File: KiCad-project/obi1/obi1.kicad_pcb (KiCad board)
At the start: 4 copper layers, 64 x 70 mm, 134 parts, among them IC1 RAM, IC2 DAC, IC3 IMU, IC4 FLASH, J1 USB, J2 JTAG-H, J3 Conn_01x04, J4 Conn_01x04, J5 Conn_01x10, J6 Conn_01x10, J7 Conn_02x11_Counter_Clockwise, J8 Conn_02x17_Counter_Clockwise, SW1 SW_Push, SW2 SW_Push, SW3 SW_DIP_x08, U1 RG3V3, U2 REG1V2, U3 XC6SLX16-FTG256, U4 OSC, U5 ADC, U6 RV1, U7 RV2

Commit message: Routear
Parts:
- removed the IC3 at (177.2, 94.7)
- added C53: @0.47uF;6.3V;X5R;0402;10%, Capacitor_SMD:C_0402_1005Metric_Pad0.74x0.62mm_HandSolder, F.Cu at (153.5, 117.0)
- added C54: @0.47uF;6.3V;X5R;0402;10%, Capacitor_SMD:C_0402_1005Metric_Pad0.74x0.62mm_HandSolder, F.Cu at (156.0, 117.0)
- added C55: @4.7uF;6.3V;X5R;0805;10%, Capacitor_SMD:C_0805_2012Metric_Pad1.18x1.45mm_HandSolder, F.Cu at (194.7, 111.7)
- added R48: @100;1/4W;0805;1%, Resistor_SMD:R_0805_2012Metric_Pad1.20x1.40mm_HandSolder, F.Cu at (163.6, 113.9)
- added R49: @100;1/4W;0805;1%, Resistor_SMD:R_0805_2012Metric_Pad1.20x1.40mm_HandSolder, F.Cu at (199.5, 111.6)
- added U6: BMF055, Package_LGA:LGA-28_5.2x3.8mm_P0.5mm, F.Cu at (199.5, 94.2)
- C1: value 4.7uf -> @4.7uF;6.3V;X5R;0805;10%; footprint Capacitor_SMD:C_0805_2012Metric -> Capacitor_SMD:C_0805_2012Metric_Pad1.18x1.45mm_HandSolder
- C10, C14, C16, C19, C24, C28, C29, C30, C31, C32, C33, C36, C46, C7: value 4.7uF -> @4.7uF;6.3V;X5R;0805;10%; footprint Capacitor_SMD:C_0805_2012Metric -> Capacitor_SMD:C_0805_2012Metric_Pad1.18x1.45mm_HandSolder
- C11, C12, C17, C20, C21, C22, C25, C26, C27, C34, C35, C50, C51, C8: value 0.47uF -> @0.47uF;6.3V;X5R;0402;10%; footprint Capacitor_SMD:C_0805_2012Metric -> Capacitor_SMD:C_0402_1005Metric_Pad0.74x0.62mm_HandSolder
- C13: value 0.01uF -> @0.01uF;6.3V;X7R;0805;10%; footprint Capacitor_SMD:C_0805_2012Metric -> Capacitor_SMD:C_0805_2012Metric_Pad1.18x1.45mm_HandSolder
- C15, C18, C23, C6, C9: value 100uF -> @100uF;6.3V;X5R;1210;20%; footprint Capacitor_SMD:C_0805_2012Metric -> Capacitor_SMD:C_1210_3225Metric_Pad1.33x2.70mm_HandSolder
- C2, C3, C4, C5: value 1uf -> @1uF;6.3V;X5R;0805;10%; footprint Capacitor_SMD:C_0805_2012Metric -> Capacitor_SMD:C_0805_2012Metric_Pad1.18x1.45mm_HandSolder
- C37: value 10uF -> @10uF;6.3V;X5R;0805;20%; footprint Capacitor_SMD:C_0805_2012Metric -> Capacitor_SMD:C_0805_2012Metric_Pad1.18x1.45mm_HandSolder
- C38: value 1uF -> @1uF;6.3V;X5R;0805;10%; footprint Capacitor_SMD:C_0805_2012Metric -> Capacitor_SMD:C_0805_2012Metric_Pad1.18x1.45mm_HandSolder
- C39, C40: value 0.1uF -> @0.1uF;6.3V;X5R;0805;10%; footprint Capacitor_SMD:C_0805_2012Metric -> Capacitor_SMD:C_0805_2012Metric_Pad1.18x1.45mm_HandSolder
- C41: value 100nF -> @0.1uF;6.3V;X5R;0805;10%; footprint Capacitor_SMD:C_0805_2012Metric -> Capacitor_SMD:C_0805_2012Metric_Pad1.18x1.45mm_HandSolder
- C42: value 100nF -> @1uF;6.3V;X5R;0805;10%; footprint Capacitor_SMD:C_0805_2012Metric -> Capacitor_SMD:C_0805_2012Metric_Pad1.18x1.45mm_HandSolder
- C43: value 4.7uF -> @1uF;6.3V;X5R;0805;10%; footprint Capacitor_SMD:C_0805_2012Metric -> Capacitor_SMD:C_0805_2012Metric_Pad1.18x1.45mm_HandSolder
- C44: value 4.7uF -> @0.12uF;10V;X7R;0603;10%; footprint Capacitor_SMD:C_0805_2012Metric -> Capacitor_SMD:C_0603_1608Metric_Pad1.08x0.95mm_HandSolder
- C45: value 4.7uF -> @6800pF;10V;X7R;0603;10%; footprint Capacitor_SMD:C_0805_2012Metric -> Capacitor_SMD:C_0603_1608Metric_Pad1.08x0.95mm_HandSolder
- C47, C48, C49: value 0.47uF -> @4.7uF;6.3V;X5R;0805;10%; footprint Capacitor_SMD:C_0805_2012Metric -> Capacitor_SMD:C_0805_2012Metric_Pad1.18x1.45mm_HandSolder
- C52: value 4.7uF -> @0.47uF;6.3V;X5R;0402;10%; footprint Capacitor_SMD:C_0805_2012Metric -> Capacitor_SMD:C_0402_1005Metric_Pad0.74x0.62mm_HandSolder
- D1: value DONE -> @DONE;LED;GRE;0603; footprint LED_SMD:LED_0805_2012Metric -> LED_SMD:LED_0603_1608Metric_Pad1.05x0.95mm_HandSolder
- D2, D3, D4, D5, D6, D7, D8, D9: value G -> @LED;BLU;0603; footprint LED_SMD:LED_0805_2012Metric -> LED_SMD:LED_0603_1608Metric_Pad1.05x0.95mm_HandSolder
- R1: value 1M -> @1M;1/2W;0805;1%; footprint Resistor_SMD:R_0805_2012Metric -> Resistor_SMD:R_0805_2012Metric_Pad1.20x1.40mm_HandSolder
- R10: value 4K7 -> @4.7K;1/4W;0805;1%; footprint Resistor_SMD:R_0805_2012Metric -> Resistor_SMD:R_0805_2012Metric_Pad1.20x1.40mm_HandSolder
- R11: value 330 -> @330;1/4W;0805;1%; footprint Resistor_SMD:R_0805_2012Metric -> Resistor_SMD:R_0805_2012Metric_Pad1.20x1.40mm_HandSolder
- R12, R2, R3, R37, R38, R4, R40, R41, R5, R6, R7, R8, R9: value 100 -> @100;1/4W;0805;1%; footprint Resistor_SMD:R_0805_2012Metric -> Resistor_SMD:R_0805_2012Metric_Pad1.20x1.40mm_HandSolder
- R13, R14, R15, R16, R17, R18: value 4.7K -> @51;1/4W;0805;5%; footprint Resistor_SMD:R_0805_2012Metric -> Resistor_SMD:R_0805_2012Metric_Pad1.20x1.40mm_HandSolder
- R19: value 4.7K -> @20;1/4W;0805;1%; footprint Resistor_SMD:R_0805_2012Metric -> Resistor_SMD:R_0805_2012Metric_Pad1.20x1.40mm_HandSolder; moved to F.Cu
- R20: value 4.7K -> @10K;1/4W;0805;1%; footprint Resistor_SMD:R_0805_2012Metric -> Resistor_SMD:R_0805_2012Metric_Pad1.20x1.40mm_HandSolder
- R21, R22, R23, R24, R25, R26: value 50 -> @4.7K;1/4W;0805;1%; footprint Resistor_SMD:R_0805_2012Metric -> Resistor_SMD:R_0805_2012Metric_Pad1.20x1.40mm_HandSolder
- R27, R28: value 20 -> @4.7K;1/4W;0805;1%; footprint Resistor_SMD:R_0805_2012Metric -> Resistor_SMD:R_0805_2012Metric_Pad1.20x1.40mm_HandSolder
- R29, R30, R31, R32, R33, R34, R35: value 100 -> @20;1/4W;0805;1%; footprint Resistor_SMD:R_0805_2012Metric -> Resistor_SMD:R_0805_2012Metric_Pad1.20x1.40mm_HandSolder; moved to B.Cu
- R36: value 100 -> @20;1/4W;0805;1%; footprint Resistor_SMD:R_0805_2012Metric -> Resistor_SMD:R_0805_2012Metric_Pad1.20x1.40mm_HandSolder
- R39: value 2K4 -> @100;1/4W;0805;1%; footprint Resistor_SMD:R_0805_2012Metric -> Resistor_SMD:R_0805_2012Metric_Pad1.20x1.40mm_HandSolder
- R42, R43, R44, R45, R46: value 20 -> @100;1/4W;0805;1%; footprint Resistor_SMD:R_0805_2012Metric -> Resistor_SMD:R_0805_2012Metric_Pad1.20x1.40mm_HandSolder; moved to F.Cu
- R47: value 20 -> @2.4K;1/4W;0805;1%; footprint Resistor_SMD:R_0805_2012Metric -> Resistor_SMD:R_0805_2012Metric_Pad1.20x1.40mm_HandSolder; moved to F.Cu
- moved R19 75.1 mm to (203.1, 98.5), turned to 0 degrees
- moved R24 68.1 mm to (128.7, 112.4)
- moved R18 66.5 mm to (180.7, 68.5)
- moved R14 65.0 mm to (173.9, 73.4)
- moved R23 65.0 mm to (128.7, 115.1), turned to 180 degrees
- moved R17 63.1 mm to (174.0, 68.5), turned to 0 degrees
- moved R26 56.7 mm to (128.7, 107.6)
- moved R25 54.1 mm to (128.7, 109.9)
- moved R16 52.9 mm to (180.6, 125.3), turned to 0 degrees
- moved R13 52.5 mm to (181.1, 122.9)
- moved R22 52.5 mm to (128.7, 117.7), turned to 180 degrees
- moved R15 51.5 mm to (179.1, 128.4), turned to 0 degrees
- moved R21 51.1 mm to (128.7, 120.1), turned to 180 degrees
- moved C52 47.1 mm to (175.5, 74.2), turned to 180 degrees
- moved C44 43.7 mm to (210.0, 92.7), turned to 0 degrees
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- renumbered IC4 to IC3, J8 to J7, J7 to J8, U6 to U7, U7 to U8
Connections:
- C43 pad 1: +3V3 -> Net-(C43-Pad1)
- C45 pad 1: +5V -> +3V3
- C46 pad 1: +5V -> +3V3
- C48 pad 1: +3V3 -> +5V
- C50 pad 1: +5V -> +3V3
- C51 pad 1: GND -> +3V3
- C51 pad 2: +3V3 -> GND
- C52 pad 1: GND -> +5V
- C52 pad 2: +3V3 -> GND
- F1 pad 2: Net-(F1-Pad2) -> (no net)
- IC3 pad 2: Net-(IC4-Pad2) -> Net-(IC3-Pad2)
- IC3 pad 3: Net-(IC4-Pad3) -> Net-(IC3-Pad3)
- IC3 pad 5: Net-(IC4-Pad5) -> Net-(IC3-Pad5)
- IC3 pad 7: Net-(IC4-Pad7) -> Net-(IC3-Pad7)
- J1 pad 4: Net-(F1-Pad2) -> +5V
- J7 pad 1: IO_C02 -> (no net)
- J7 pad 2: IO_C04 -> (no net)
- J7 pad 3: IO_C06 -> (no net)
- J7 pad 4: IO_C03 -> (no net)
- J8 pad 3: IO_C00 -> (no net)
- J8 pad 5: IO_C01 -> (no net)
- R13 pad 1: DS_1 -> Net-(IC2-Pad4)
- R13 pad 2: GND -> DAC_SCK
- R14 pad 1: DS_2 -> Net-(R14-Pad1)
- R14 pad 2: GND -> ADC_SCLK
- R15 pad 1: DS_3 -> Net-(J3-Pad1)
- R15 pad 2: GND -> DAC_VOUTA
- R16 pad 1: DS_4 -> Net-(J3-Pad4)
- R16 pad 2: GND -> DAC_VOUTB
- R17 pad 1: DS_5 -> Net-(J4-Pad1)
- R17 pad 2: GND -> ADC_IN1
- R18 pad 1: DS_6 -> Net-(J4-Pad4)
- R18 pad 2: GND -> ADC_IN2
- R19 pad 1: DS_7 -> +3V3
- R19 pad 2: GND -> nReset
- R20 pad 1: DS_8 -> Net-(R20-Pad1)
- R20 pad 2: GND -> +3V3
- R21 pad 1: Net-(J3-Pad1) -> DS_1
- R21 pad 2: DAC_VOUTA -> GND
- R22 pad 1: Net-(J3-Pad4) -> DS_2
- R22 pad 2: DAC_VOUTB -> GND
- R23 pad 1: Net-(J4-Pad1) -> DS_3
- R23 pad 2: ADC_IN1 -> GND
- R24 pad 1: Net-(J4-Pad4) -> DS_4
- R24 pad 2: ADC_IN2 -> GND
- R25 pad 1: Net-(IC2-Pad4) -> DS_5
- R25 pad 2: DAC_SCK -> GND
- R26 pad 1: Net-(R26-Pad1) -> DS_6
- R26 pad 2: ADC_SCLK -> GND
- R27 pad 1: IO_B03 -> DS_7
- R27 pad 2: DS_1 -> GND
- R28 pad 1: IO_B05 -> DS_8
- R28 pad 2: DS_2 -> GND
- R29 pad 1: Net-(D2-Pad2) -> IO_B03
- R29 pad 2: LED_1 -> DS_1
- R30 pad 1: Net-(D3-Pad2) -> IO_B05
- R30 pad 2: LED_2 -> DS_2
- R31 pad 1: Net-(D4-Pad2) -> IO_D04
- R31 pad 2: LED_3 -> DS_3
- R32 pad 1: Net-(D5-Pad2) -> IO_A07
- R32 pad 2: LED_4 -> DS_4
- R33 pad 1: Net-(D6-Pad2) -> IO_A04
- R33 pad 2: LED_5 -> DS_5
- R34 pad 1: Net-(D7-Pad2) -> IO_B00
- R34 pad 2: LED_6 -> DS_6
- R35 pad 1: Net-(D8-Pad2) -> IO_D01
- R35 pad 2: LED_7 -> DS_7
- R36 pad 1: Net-(D9-Pad2) -> IO_D05
- R36 pad 2: LED_8 -> DS_8
- R37 pad 1: Net-(IC4-Pad3) -> Net-(D2-Pad2)
- R37 pad 2: XC_N12 -> LED_1
- R38 pad 1: Net-(IC4-Pad2) -> Net-(D3-Pad2)
- R38 pad 2: XC_P10 -> LED_2
- R39 pad 1: +3V3 -> Net-(D4-Pad2)
- R39 pad 2: XC_T3 -> LED_3
- R40 pad 1: XC_P12 -> Net-(D5-Pad2)
- R40 pad 2: Net-(IC4-Pad7) -> LED_4
- R41 pad 1: XC_T10 -> Net-(D6-Pad2)
- R41 pad 2: Net-(IC4-Pad5) -> LED_5
- R42 pad 1: IO_D04 -> Net-(D7-Pad2)
- R42 pad 2: DS_3 -> LED_6
- R43 pad 1: IO_A07 -> Net-(D8-Pad2)
- R43 pad 2: DS_4 -> LED_7
- R44 pad 1: IO_A04 -> Net-(D9-Pad2)
- R44 pad 2: DS_5 -> LED_8
- R45 pad 1: IO_B00 -> Net-(IC3-Pad3)
- R45 pad 2: DS_6 -> XC_N12
- R46 pad 1: IO_D01 -> Net-(IC3-Pad2)
- R46 pad 2: DS_7 -> XC_P10
- R47 pad 1: IO_D05 -> +3V3
- R47 pad 2: DS_8 -> XC_T3
- U3 pad A9: OSC_ED -> (no net)
- U3 pad C15: IMU_CSB2 -> IMU_PA31
- U3 pad C16: IMU_DRDYM -> IMU_PA30
- U3 pad D16: IMU_INT2 -> IMU_PA18
- U3 pad E13: IO_C06 -> nReset
- U3 pad E15: IMU_INT1 -> IMU_PA28
- U3 pad E16: IMU_CSB3 -> IMU_PA27
- U3 pad F12: (no net) -> IMU_PB00
- U3 pad F13: IO_C03 -> IMU_PA17
- U3 pad F14: IO_C02 -> IMU_PA16
- U3 pad F15: IMU_CSB1 -> IMU_PA24
- U3 pad F16: IMU_MISO -> IMU_PA23
- U3 pad G11: IO_C04 -> IMU_PB01
- U3 pad G12: (no net) -> IMU_PB02
- U3 pad G14: IMU_INT3 -> IMU_PA22
- U3 pad G16: IMU_INT4 -> IMU_PA21
- U3 pad H11: IO_C00 -> IMU_PB03
- U3 pad H13: IO_C01 -> IMU_PB16
- U3 pad H15: IMU_INT5 -> IMU_PA20
- U3 pad H16: IMU_SDX -> IMU_PA19
- U3 pad J12: (no net) -> IMU_PB17
- U3 pad J14: (no net) -> IMU_PB23
- U4 pad 1: OSC_ED -> +3V3
- U5 pad 8: Net-(R26-Pad1) -> Net-(R14-Pad1)
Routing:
- net IO_C00: track 72.3 -> 0.00 mm, vias 1 -> 0
- net IMU_PB03: track 0.00 -> 72.3 mm, vias 0 -> 1
- net IO_C01: track 70.4 -> 0.00 mm, vias 1 -> 0
- net IMU_PB16: track 0.00 -> 70.4 mm, vias 0 -> 1
- net nReset: track 0.00 -> 59.1 mm, vias 0 -> 9
- net IO_C04: track 35.3 -> 0.00 mm, vias 1 -> 0
- net IMU_PB01: track 0.00 -> 35.3 mm, vias 0 -> 1
- net IO_C03: track 33.4 -> 0.00 mm, vias 1 -> 0
- net IMU_PA17: track 0.00 -> 33.4 mm, vias 0 -> 1
- net IO_C02: track 28.8 -> 0.00 mm, vias 1 -> 0
- net IMU_PA16: track 0.00 -> 28.8 mm, vias 0 -> 1
- net IO_C06: track 28.7 -> 0.00 mm, vias 1 -> 0
- net +3V3: track 157.6 -> 130.7 mm, vias 89 -> 79
- net IMU_PA31: track 0.00 -> 17.4 mm
- net IMU_CSB2: track 17.4 -> 0.00 mm
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- added copper zone on VCC, net nReset
- removed copper zone on VCC, net +3V3
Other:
- net class Default: clearance 0.1321 -> 0.1524; trace_width 0.1321 -> 0.1524; via_dia 0.4 -> 0.61; via_drill 0.2 -> 0.3
- net class PWR: clearance 0.127 -> 0.1524; trace_width 0.381 -> 0.4; via_dia 0.4 -> 0.61; via_drill 0.2 -> 0.3
- rule trace_clearance: 0.1321 -> 0.1524
- rule trace_min: 0.13 -> 0.1524
- rule via_min_drill: 0.2 -> 0.3
- rule via_min_size: 0.4 -> 0.61

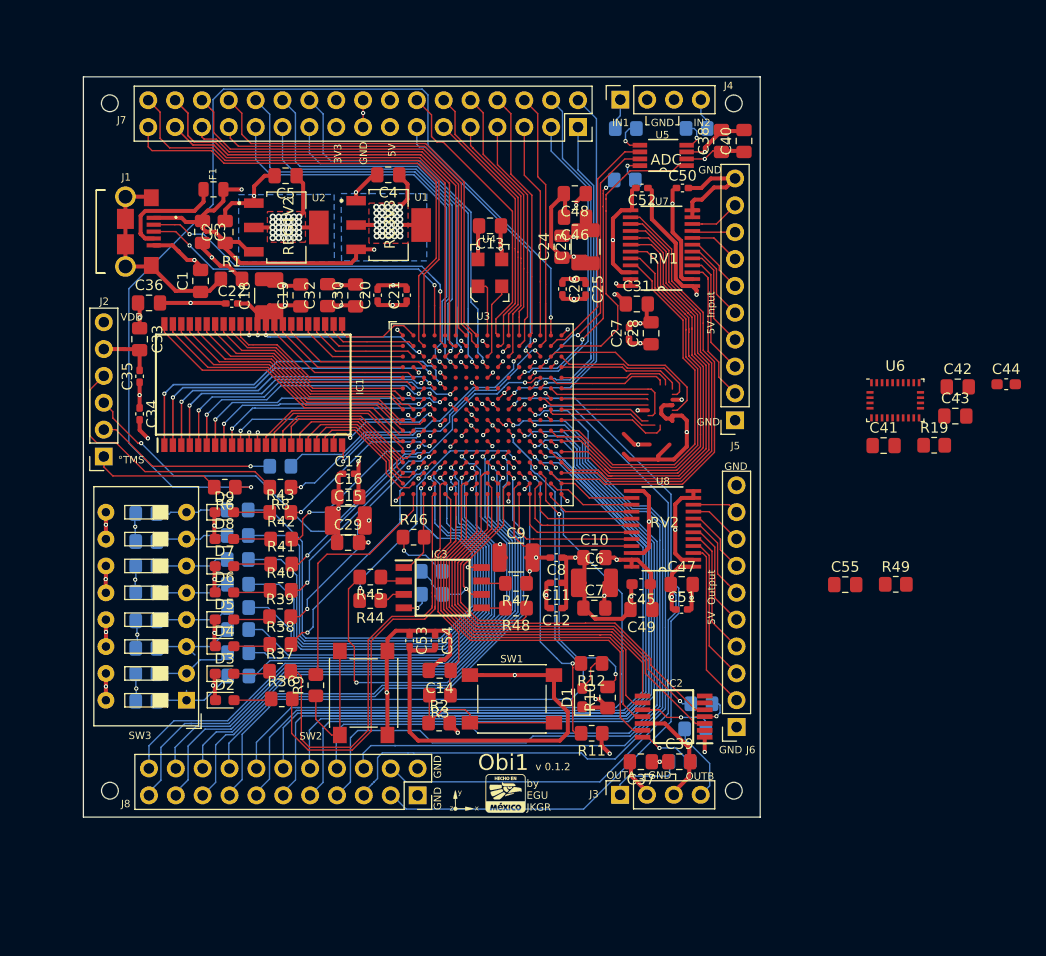
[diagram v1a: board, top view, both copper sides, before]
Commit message: Resize board, change layout, re-route IO pins, new imu added
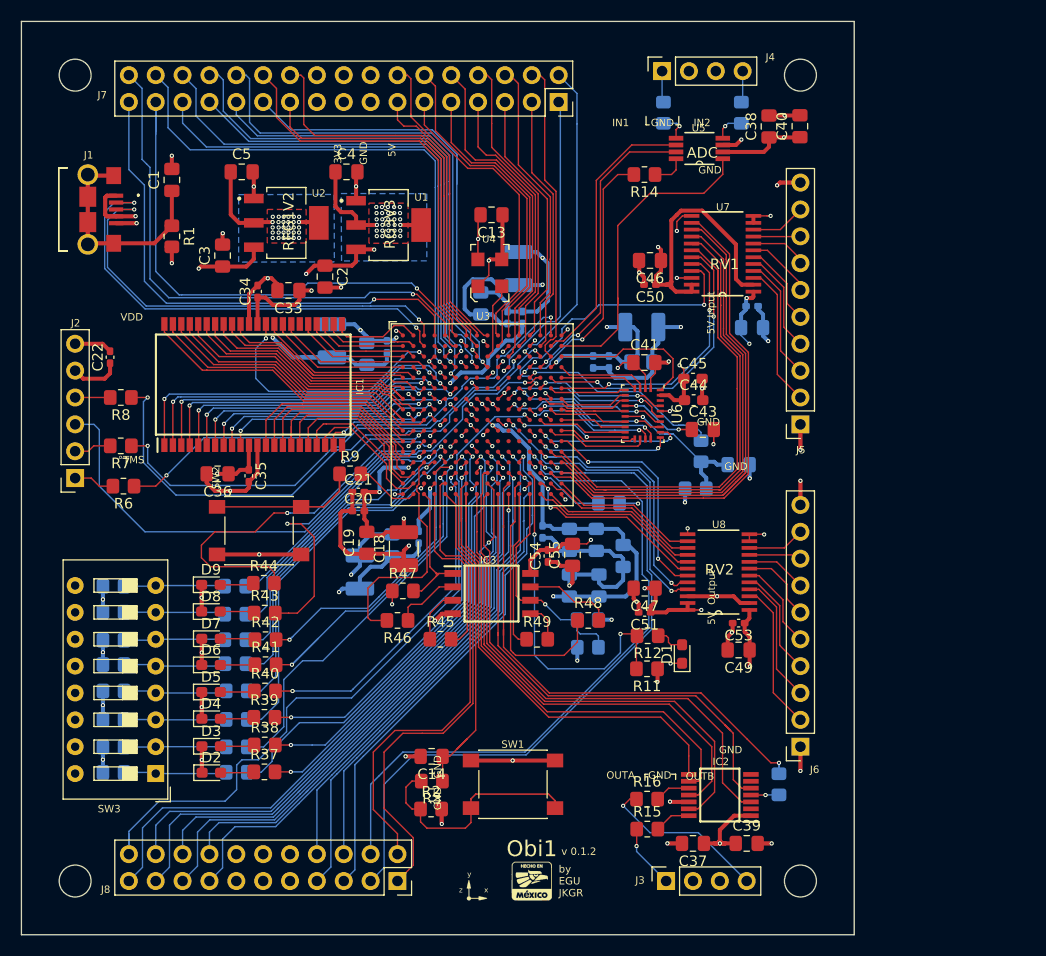
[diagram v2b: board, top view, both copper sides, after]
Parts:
- removed F1: Fuse, Fuse:Fuse_0805_2012Metric
- C10, C11, C12, C15, C16, C17, C23, C24, C25, C26, C27, C28, C29, C30, C31, C32, C42, C48, C52, C6, C7, C8, C9, R10, R36: moved to B.Cu
- R14, R15, R16, R7: moved to F.Cu
- R19: value @20;1/4W;0805;1% -> @10;1/4W;0805;1%; moved to B.Cu
- moved R20 55.7 mm to (180.6, 102.6), turned to 0 degrees
- moved C32 35.7 mm to (168.7, 111.8), turned to 270 degrees
- moved C30 35.3 mm to (173.7, 109.0)
- moved R49 34.3 mm to (165.6, 116.8)
- moved C6 33.8 mm to (146.2, 88.6), turned to 90 degrees
- moved C7 32.3 mm to (149.5, 89.9), turned to 90 degrees
- moved C53 31.2 mm to (184.7, 115.3), turned to 180 degrees
- moved C44 29.6 mm to (180.4, 94.2)
- moved C18 27.1 mm to (153.0, 108.3)
- moved C31 26.9 mm to (171.4, 111.8), turned to 270 degrees
- moved C55 25.9 mm to (168.9, 108.9), turned to 90 degrees
- moved C8 25.6 mm to (151.4, 89.2), turned to 90 degrees
- moved C9 24.8 mm to (175.5, 87.3), turned to 180 degrees
- moved C19 24.2 mm to (149.5, 107.7)
- moved C41 23.9 mm to (175.7, 90.7)
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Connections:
- C42 pad 1: +3V3 -> Net-(C42-Pad1)
- J7 pad 1: (no net) -> IO_C01
- J7 pad 10: IO_I00 -> IO_D03
- J7 pad 11: IO_G03 -> IO_D04
- J7 pad 12: IO_H04 -> IO_D05
- J7 pad 13: IO_I01 -> IO_D06
- J7 pad 14: IO_G04 -> IO_D07
- J7 pad 15: +5V -> +3V3
- J7 pad 16: +5V -> +3V3
- J7 pad 19: +3V3 -> +5V
- J7 pad 2: (no net) -> IO_C02
- J7 pad 20: +3V3 -> +5V
- J7 pad 21: IO_H01 -> IO_E01
- J7 pad 22: IO_H06 -> IO_E02
- J7 pad 23: IO_F00 -> IO_E03
- J7 pad 24: IO_G00 -> IO_E04
- J7 pad 25: IO_E07 -> IO_E05
- J7 pad 26: IO_F07 -> IO_E06
- J7 pad 27: IO_G01 -> IO_E07
- J7 pad 28: IO_G02 -> IO_F01
- J7 pad 3: (no net) -> IO_C03
- J7 pad 30: IO_F06 -> IO_F03
- J7 pad 31: IO_D02 -> IO_F04
- J7 pad 32: IO_F01 -> IO_F05
- J7 pad 33: IO_B04 -> IO_F06
- J7 pad 34: IO_B07 -> IO_F07
- J7 pad 4: (no net) -> IO_C04
- J7 pad 5: IO_I06 -> IO_C05
- J7 pad 6: IO_I05 -> IO_C06
- J7 pad 7: IO_H07 -> IO_C07
- J7 pad 8: IO_I02 -> IO_D01
- J7 pad 9: IO_H03 -> IO_D02
- J8 pad 1: GND -> IO_A00
- J8 pad 10: IO_E04 -> +3V3
- J8 pad 11: IO_E02 -> GND
- J8 pad 12: IO_E06 -> GND
- J8 pad 13: IO_E05 -> +5V
- J8 pad 14: IO_E01 -> +5V
- J8 pad 15: DS_2_XC7 -> IO_B00
- J8 pad 16: IO_A02 -> IO_B01
- J8 pad 17: IO_A01 -> IO_B02
- J8 pad 18: IO_A03 -> IO_B03
- J8 pad 19: IO_A06 -> IO_B04
- J8 pad 2: GND -> IO_A01
- J8 pad 20: IO_B01 -> IO_B05
- J8 pad 22: IO_B02 -> IO_B07
- J8 pad 3: (no net) -> IO_A02
- J8 pad 4: DS_2_XC1 -> IO_A03
- J8 pad 5: (no net) -> IO_A04
- J8 pad 6: DS_2_XC2 -> IO_A05
- J8 pad 7: DS_2_XC4 -> IO_A06
- J8 pad 8: DS_2_XC6 -> IO_A07
- J8 pad 9: DS_2_XC5 -> +3V3
- R19 pad 1: +3V3 -> Net-(C42-Pad1)
- R20 pad 1: Net-(R20-Pad1) -> +3V3
- R20 pad 2: +3V3 -> Net-(C42-Pad1)
- R29 pad 1: IO_B03 -> DS_2_XC1
- R30 pad 1: IO_B05 -> DS_2_XC2
- R31 pad 1: IO_D04 -> DS_2_XC3
- R32 pad 1: IO_A07 -> DS_2_XC4
- R33 pad 1: IO_A04 -> DS_2_XC5
- R34 pad 1: IO_B00 -> DS_2_XC6
- R35 pad 1: IO_D01 -> DS_2_XC7
- R36 pad 1: IO_D05 -> DS_2_XC8
- U3 pad A10: IO_G04 -> IO_D04
- U3 pad A11: IO_H04 -> IO_D02
- U3 pad A12: IO_I00 -> IO_C07
- U3 pad A13: IO_I02 -> IO_C05
- U3 pad A14: IO_I06 -> IO_C06
- U3 pad A3: IO_B07 -> D+
- U3 pad A4: D+ -> IO_F06
- U3 pad A5: IO_D02 -> IO_F07
- U3 pad A6: IO_F02 -> IO_E04
- U3 pad A7: IO_F06 -> IO_E01
- U3 pad A8: IO_G02 -> IO_D06
- U3 pad A9: (no net) -> IO_D07
- U3 pad B10: IO_G03 -> IO_D05
- U3 pad B12: IO_H07 -> IO_D01
- U3 pad B14: IO_I05 -> IO_C03
- U3 pad B3: IO_B04 -> D-
- U3 pad B5: D- -> (no net)
- U3 pad B6: IO_F01 -> IO_F04
- U3 pad B8: IO_G01 -> IO_E02
- U3 pad C11: IO_H03 -> IO_D03
- U3 pad C13: IO_I01 -> IO_C02
- U3 pad C15: IMU_PA31 -> IO_C04
- U3 pad C16: IMU_PA30 -> IMU_PB03
- U3 pad C5: IO_F00 -> IO_F03
- U3 pad C6: IO_G00 -> IO_F01
- U3 pad C8: (no net) -> IO_E06
- U3 pad D11: (no net) -> IO_C01
- U3 pad D16: IMU_PA18 -> IMU_PB02
- U3 pad D5: IO_E07 -> IO_F05
- U3 pad D6: IO_F07 -> IO_F02
- U3 pad D8: IO_H01 -> IO_E05
- U3 pad D9: IO_H06 -> IO_E03
- U3 pad E15: IMU_PA28 -> 3v3_2_XC02
- U3 pad E16: IMU_PA27 -> IMU_PB01
- U3 pad E6: (no net) -> IO_E07
- U3 pad F12: IMU_PB00 -> IMU_PA17
- U3 pad F13: IMU_PA17 -> 3v3_2_XC00
- U3 pad F14: IMU_PA16 -> IMU_SCX
- U3 pad F15: IMU_PA24 -> IMU_PB00
- U3 pad F16: IMU_PA23 -> 3v3_2_XC01
- U3 pad G11: IMU_PB01 -> IMU_PA16
- U3 pad G12: IMU_PB02 -> (no net)
- U3 pad G14: IMU_PA22 -> IMU_PA30
- U3 pad G16: IMU_PA21 -> IMU_PA31
- U3 pad H11: IMU_PB03 -> IMU_PA18
- U3 pad H13: IMU_PB16 -> IMU_PA20
- U3 pad H14: DS_2_XC1 -> IMU_PB17
- U3 pad H15: IMU_PA20 -> IMU_PA27
- U3 pad H16: IMU_PA19 -> IMU_PA28
- U3 pad J11: DS_2_XC2 -> 3v3_2_XC08
- U3 pad J12: IMU_PB17 -> IMU_PA23
- U3 pad J13: DS_2_XC4 -> IO_B07
- U3 pad J14: IMU_PB23 -> IMU_PA24
- U3 pad J16: IMU_SCX -> IMU_PB23
- U3 pad K11: DS_2_XC7 -> (no net)
- U3 pad K12: DS_2_XC6 -> (no net)
- U3 pad K14: DS_2_XC5 -> IMU_PA19
- U3 pad K15: 3v3_2_XC01 -> IMU_PA21
- U3 pad K16: 3v3_2_XC00 -> IMU_PA22
- U3 pad L13: IO_E04 -> (no net)
- U3 pad L14: IO_E02 -> IMU_PB16
- U3 pad L16: 3v3_2_XC02 -> 3v3_2_XC10
- U3 pad M10: IO_A06 -> IO_B01
- U3 pad M11: IO_A01 -> IO_A06
- U3 pad M13: IO_E05 -> IO_A03
- U3 pad M14: IO_E06 -> 3v3_2_XC09
- U3 pad M3: LED_6 -> DS_2_XC8
- U3 pad M4: LED_5 -> DS_2_XC7
- U3 pad M5: (no net) -> DS_2_XC6
- U3 pad M6: (no net) -> LED_6
- U3 pad M7: IO_B06 -> LED_2
- U3 pad M9: IO_B01 -> IO_B03
- U3 pad N11: GND -> (no net)
- U3 pad N12: XC_N12 -> IO_A04
- U3 pad N14: IO_E01 -> IO_A02
- U3 pad N3: LED_4 -> XC_P10
- U3 pad N4: LED_3 -> DS_2_XC5
- U3 pad N5: IO_B00 -> DS_2_XC4
- U3 pad N6: IO_D04 -> DS_2_XC1
- U3 pad N8: IO_B02 -> IO_B06
- U3 pad N9: IO_A03 -> IO_B04
- U3 pad P10: XC_P10 -> IO_B02
- U3 pad P11: IO_A02 -> IO_A07
- U3 pad P12: XC_P12 -> IO_A05
- U3 pad P4: IO_D01 -> DS_2_XC2
- U3 pad P5: IO_A04 -> LED_5
- U3 pad P6: IO_A07 -> LED_4
- U3 pad P7: IO_B05 -> LED_3
- U3 pad P8: IO_B03 -> LED_1
- U3 pad P9: DAC_CS -> DAC_VREFA
- U3 pad R11: XC_R11 -> DAC_SCK
- U3 pad R12: 3v3_2_XC08 -> XC_P12
- U3 pad R3: IO_D05 -> DS_2_XC3
- U3 pad R5: LED_1 -> IO_A01
- U3 pad R7: DAC_VREFB -> DAC_LDAC
- U3 pad R9: DAC_SDI -> IO_B05
- U3 pad T10: XC_T10 -> DAC_SDI
- U3 pad T11: +3V3 -> IO_B00
- U3 pad T12: 3v3_2_XC09 -> XC_T10
- U3 pad T13: 3v3_2_XC10 -> XC_R11
- U3 pad T4: LED_2 -> XC_N12
- U3 pad T5: XC_RST -> IO_A00
- U3 pad T6: DAC_VREFA -> XC_RST
- U3 pad T8: DAC_LDAC -> DAC_VREFB
- U3 pad T9: DAC_SCK -> DAC_CS
- U6 pad 11: Net-(R20-Pad1) -> Net-(C42-Pad1)
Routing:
- net +3V3: track 130.7 -> 221.2 mm, vias 79 -> 81
- net IO_E02: track 127.5 -> 39.5 mm, vias 1 -> 0
- net IO_E06: track 120.5 -> 46.8 mm
- net +5V: track 143.4 -> 213.3 mm, vias 6 -> 7
- net IMU_PB16: track 70.4 -> 12.7 mm, vias 1 -> 2
- net IMU_PB03: track 72.3 -> 15.1 mm, vias 1 -> 0
- net IO_F04: track 0.00 -> 55.3 mm, vias 0 -> 1
- net IO_F05: track 0.00 -> 51.9 mm, vias 0 -> 1
- net TMS: track 99.1 -> 49.0 mm
- net IO_F03: track 0.00 -> 48.5 mm, vias 0 -> 1
- net IO_A00: track 0.00 -> 45.1 mm
- net IO_E03: track 0.00 -> 44.5 mm, vias 0 -> 1
- net IO_A05: track 0.00 -> 43.8 mm, vias 0 -> 1
- net IO_G02: track 41.6 -> 0.00 mm
- net IO_G01: track 40.7 -> 0.00 mm
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- added copper zone on VCC, net +3V3
- removed copper zone on VCC, net nReset
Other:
- board size 64 x 70 mm -> 78.7 x 86.4 mm
- net class Default: clearance 0.1524 -> 0.132121; trace_width 0.1524 -> 0.132121; via_dia 0.61 -> 0.4; via_drill 0.3 -> 0.2
- net class PWR: clearance 0.1524 -> 0.132121; trace_width 0.4 -> 0.381; via_dia 0.61 -> 0.4; via_drill 0.3 -> 0.2
- rule trace_clearance: 0.1524 -> 0.132121
- rule trace_min: 0.1524 -> 0.132121
- rule via_min_drill: 0.3 -> 0.2
- rule via_min_size: 0.61 -> 0.4

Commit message: Text in  Silk layer adjusted
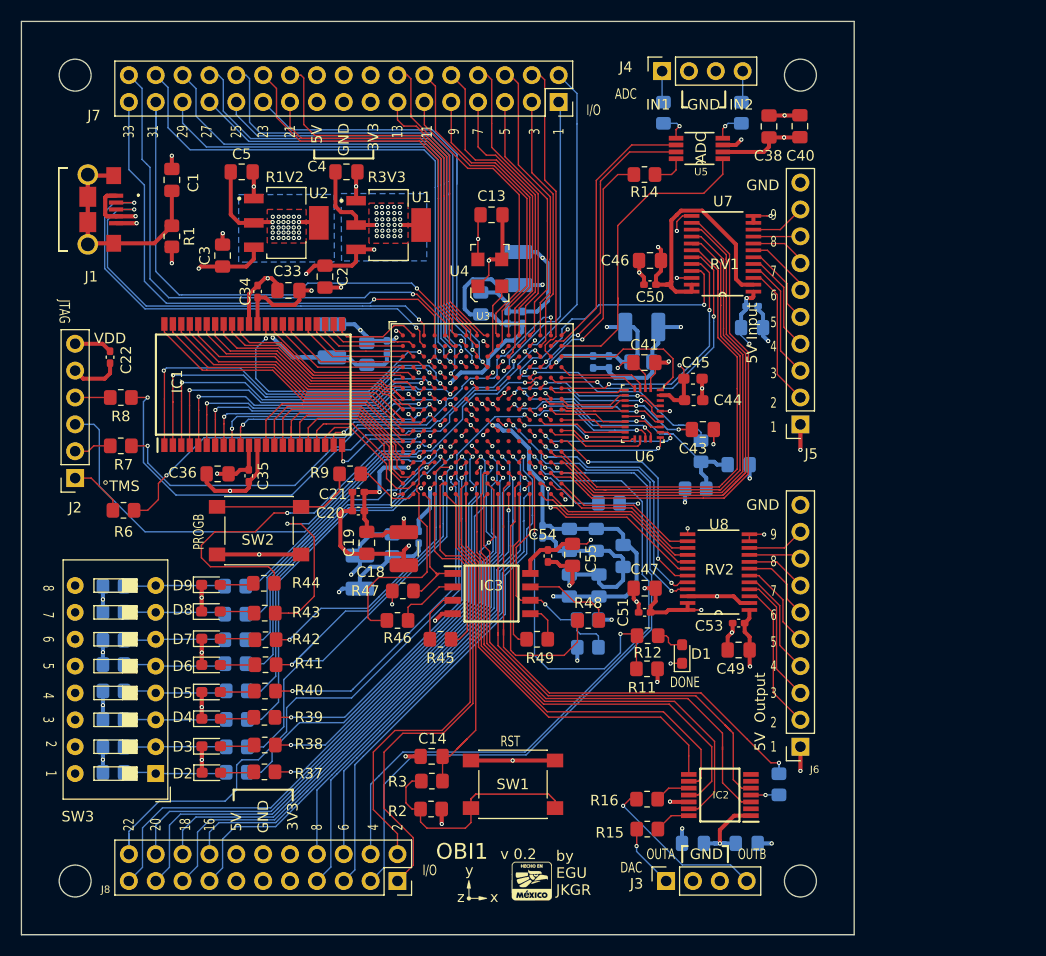
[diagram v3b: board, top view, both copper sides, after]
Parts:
- C37, C39: moved to B.Cu
- U1: value RG3V3 -> R3V3
- U2: value REG1V2 -> R1V2
- moved G*** 3.39 mm to (160.5, 97.8)
- moved R6 2.29 mm to (126.5, 104.6)
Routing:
- net GND: track 242.5 -> 237.9 mm, vias 79 -> 77
- net RAM_A0: track 33.5 -> 37.2 mm
- net RAM_A1: track 30.5 -> 33.7 mm
- net RAM_A2: track 29.3 -> 31.7 mm
- net TMS: track 49.0 -> 50.8 mm
- net RAM_A3: track 27.2 -> 29.0 mm
- net Net-(J2-Pad1): track 4.97 -> 6.50 mm
- net RAM_A4: track 29.0 -> 30.5 mm
- net RAM_CE: track 24.8 -> 25.8 mm
- net RAM_IO0: track 25.2 -> 26.0 mm
- net +3V3: track 221.2 -> 220.5 mm
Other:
- board text added: "1"
- board text added: "11"
- board text added: "13"
- board text added: "16"
- board text added: "18"
- board text added: "2"
- board text added: "20"
- board text added: "21"
- board text added: "22"
- board text added: "23"
- board text added: "25"
- board text added: "27"
- board text added: "29"
- board text added: "3"
- board text added: "31"
- board text added: "33"
- board text added: "4"
- board text added: "5"
- board text added: "6"
- board text added: "7"
- board text added: "8"
- board text added: "9"
- board text added: "ADC"
- board text added: "DAC"
- board text added: "DONE"
- board text added: "I/O"
- board text added: "JTAG"
- board text added: "OBI1"
- board text added: "PROGB"
- board text added: "RST"
- board text added: "v 0.2"
- board text removed: "Obi1"
- board text removed: "v 0.1.2"
